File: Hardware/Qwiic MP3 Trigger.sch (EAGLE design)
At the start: 55 parts, among them J1 MICRO-SD, J3 PTH, J7 ISP, J8 3.5mm Audio, J9 Poke-Home, U1 TPA2005D1, U2 WT2003S, U3 AP2112-3.3V, U4 ATTINY84-ARDUINO

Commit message: File name clean up.
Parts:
- removed U$1: SPARKX-LOGO3, SparkX:SPARKX-LOGO3
- removed U$2: SPARKX-LOGO4, SparkX:SPARKX-LOGO4
- added LOGO2: SFE_LOGO_NAME.1_INCH, SparkFun-Aesthetics:SFE_LOGO_NAME.1_INCH
- added LOGO3: SFE_LOGO_NAME_FLAME.1_INCH, SparkFun-Aesthetics:SFE_LOGO_NAME_FLAME.1_INCH
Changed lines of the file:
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@@
 <class number="0" name="default" width="0" drill="0">
 </class>
-<class number="1" name="3.3V" width="0.1524" drill="0">
+<class number="1" name="3.3V" width="0.3048" drill="0">
 </class>
 </classes>
@@
 <part name="GND7" library="SparkFun-PowerSymbols" deviceset="GND" device=""/>
 <part name="FRAME1" library="SparkFun-Aesthetics" deviceset="FRAME-LETTER" device=""/>
-<part name="U$2" library="SparkX" deviceset="SPARKX-LOGO" device="4"/>
 <part name="SUPPLY8" library="SparkFun-PowerSymbols" deviceset="3.3V" device=""/>
 <part name="J4" library="SparkFun-Connectors" deviceset="QWIIC_CONNECTOR" device="JS-1MM"/>
 <part name="GND8" library="SparkFun-PowerSymbols" deviceset="GND" device=""/>
 <part name="LOGO1" library="SparkFun-Aesthetics" deviceset="OSHW-LOGO" device="MINI"/>
-<part name="U$1" library="SparkX" deviceset="SPARKX-LOGO" device="3" value="SPARKX-LOGO3"/>
 <part name="J5" library="SparkFun-Connectors" deviceset="CONN_01" device="PTH_NO_SILK_YES_STOP"/>
 <part name="JP1" library="SparkFun" deviceset="FIDUCIAL" device="UFIDUCIAL"/>
@@
 <part name="GND19" library="SparkFun-PowerSymbols" deviceset="GND" device=""/>
 <part name="GND20" library="SparkFun-PowerSymbols" deviceset="GND" device=""/>
+<part name="LOGO2" library="SparkFun-Aesthetics" deviceset="SFE_LOGO_NAME" device=".1_INCH"/>
+<part name="LOGO3" library="SparkFun-Aesthetics" deviceset="SFE_LOGO_NAME_FLAME" device=".1_INCH"/>
 </parts>
 <sheets>
@@
 <attribute name="DRAWING_NAME" x="162.814" y="17.78" size="2.7432" layer="94" font="vector"/>
 </instance>
-<instance part="U$2" gate="G$1" x="121.92" y="7.62" smashed="yes"/>
 <instance part="SUPPLY8" gate="G$1" x="48.26" y="27.94" smashed="yes" rot="MR0">
 <attribute name="VALUE" x="48.26" y="30.734" size="1.778" layer="96" rot="MR0" align="bottom-center"/>
@@
 </instance>
 <instance part="LOGO1" gate="G$1" x="121.92" y="22.86" smashed="yes"/>
-<instance part="U$1" gate="G$1" x="121.92" y="7.62" smashed="yes"/>
 <instance part="J5" gate="G$1" x="88.9" y="27.94" smashed="yes" rot="MR180">
 <attribute name="VALUE" x="86.36" y="32.766" size="1.778" layer="96" font="vector" rot="MR180"/>
@@
 <attribute name="VALUE" x="88.9" y="106.68" size="1.778" layer="96"/>
 </instance>
+<instance part="LOGO2" gate="G$1" x="2.286" y="42.926" smashed="yes"/>
+<instance part="LOGO3" gate="G$1" x="3.556" y="42.418" smashed="yes"/>
 </instances>
 <busses>
 </busses>
 <nets>
-<net name="3.3V" class="0">
+<net name="3.3V" class="1">
 <segment>
 <pinref part="J2" gate="G$1" pin="2"/>

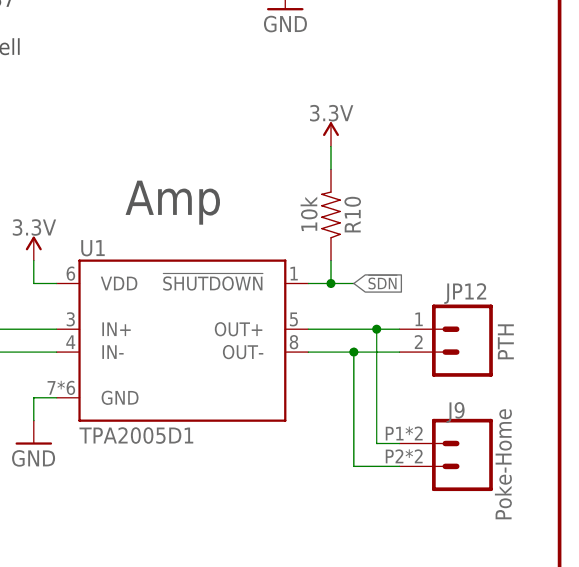
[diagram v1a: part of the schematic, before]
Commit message: Routing Playing pin on WS to Shutdown pin on amp
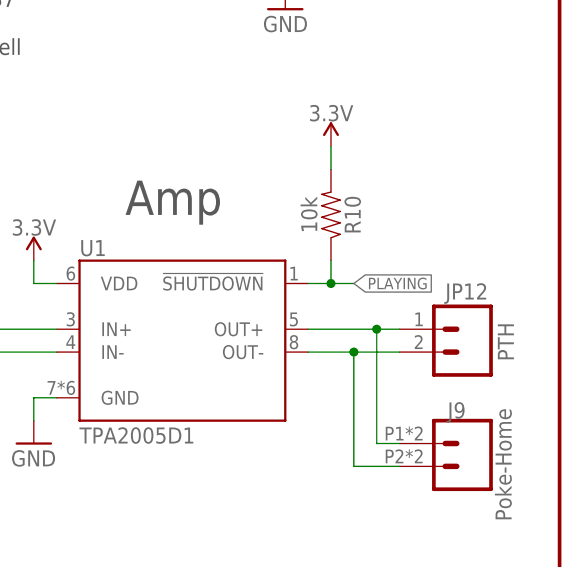
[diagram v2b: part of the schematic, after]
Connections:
- net !SDN: no longer R10.1, U1.!SHUTDOWN
- net PLAYING: now also R10.1, U1.!SHUTDOWN
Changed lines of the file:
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@@
 <net name="!SDN" class="0">
-<segment>
-<wire x1="226.06" y1="73.66" x2="223.52" y2="73.66" width="0.1524" layer="91"/>
-<wire x1="223.52" y1="73.66" x2="220.98" y2="73.66" width="0.1524" layer="91"/>
-<wire x1="223.52" y1="76.2" x2="223.52" y2="73.66" width="0.1524" layer="91"/>
-<junction x="223.52" y="73.66"/>
-<pinref part="R10" gate="G$1" pin="1"/>
-<label x="226.06" y="73.66" size="1.27" layer="95" rot="MR180" xref="yes"/>
-<pinref part="U1" gate="U1" pin="!SHUTDOWN"/>
-</segment>
 <segment>
 <pinref part="U2" gate="U1" pin="P10"/>
@@
 <pinref part="U4" gate="U1" pin="(A2)2"/>
 </segment>
+<segment>
+<wire x1="226.06" y1="73.66" x2="223.52" y2="73.66" width="0.1524" layer="91"/>
+<wire x1="223.52" y1="73.66" x2="220.98" y2="73.66" width="0.1524" layer="91"/>
+<wire x1="223.52" y1="76.2" x2="223.52" y2="73.66" width="0.1524" layer="91"/>
+<junction x="223.52" y="73.66"/>
+<pinref part="R10" gate="G$1" pin="1"/>
+<label x="226.06" y="73.66" size="1.27" layer="95" rot="MR180" xref="yes"/>
+<pinref part="U1" gate="U1" pin="!SHUTDOWN"/>
+</segment>
 </net>

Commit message: Rolling to v11 copper
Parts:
- added JP8: INT, SparkFun-Jumpers:JUMPER-SMT_2_NC_TRACE_SILK
- added R7: 10k, SparkFun-Resistors:10KOHM-0603-1/10W-1%
- JP7: device SparkFun-Jumpers:JUMPER-SMT_2_NO_NO-SILK -> SparkFun-Jumpers:JUMPER-SMT_2_NO_SILK
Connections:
- new net N$4: JP8.1, R7.2
- net !INT: now also R7.1
- net 3.3V: now also JP8.2
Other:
- moved on the sheet: C16, C2, J7, JP7, JP9, R2, R6, R8, U3, U4

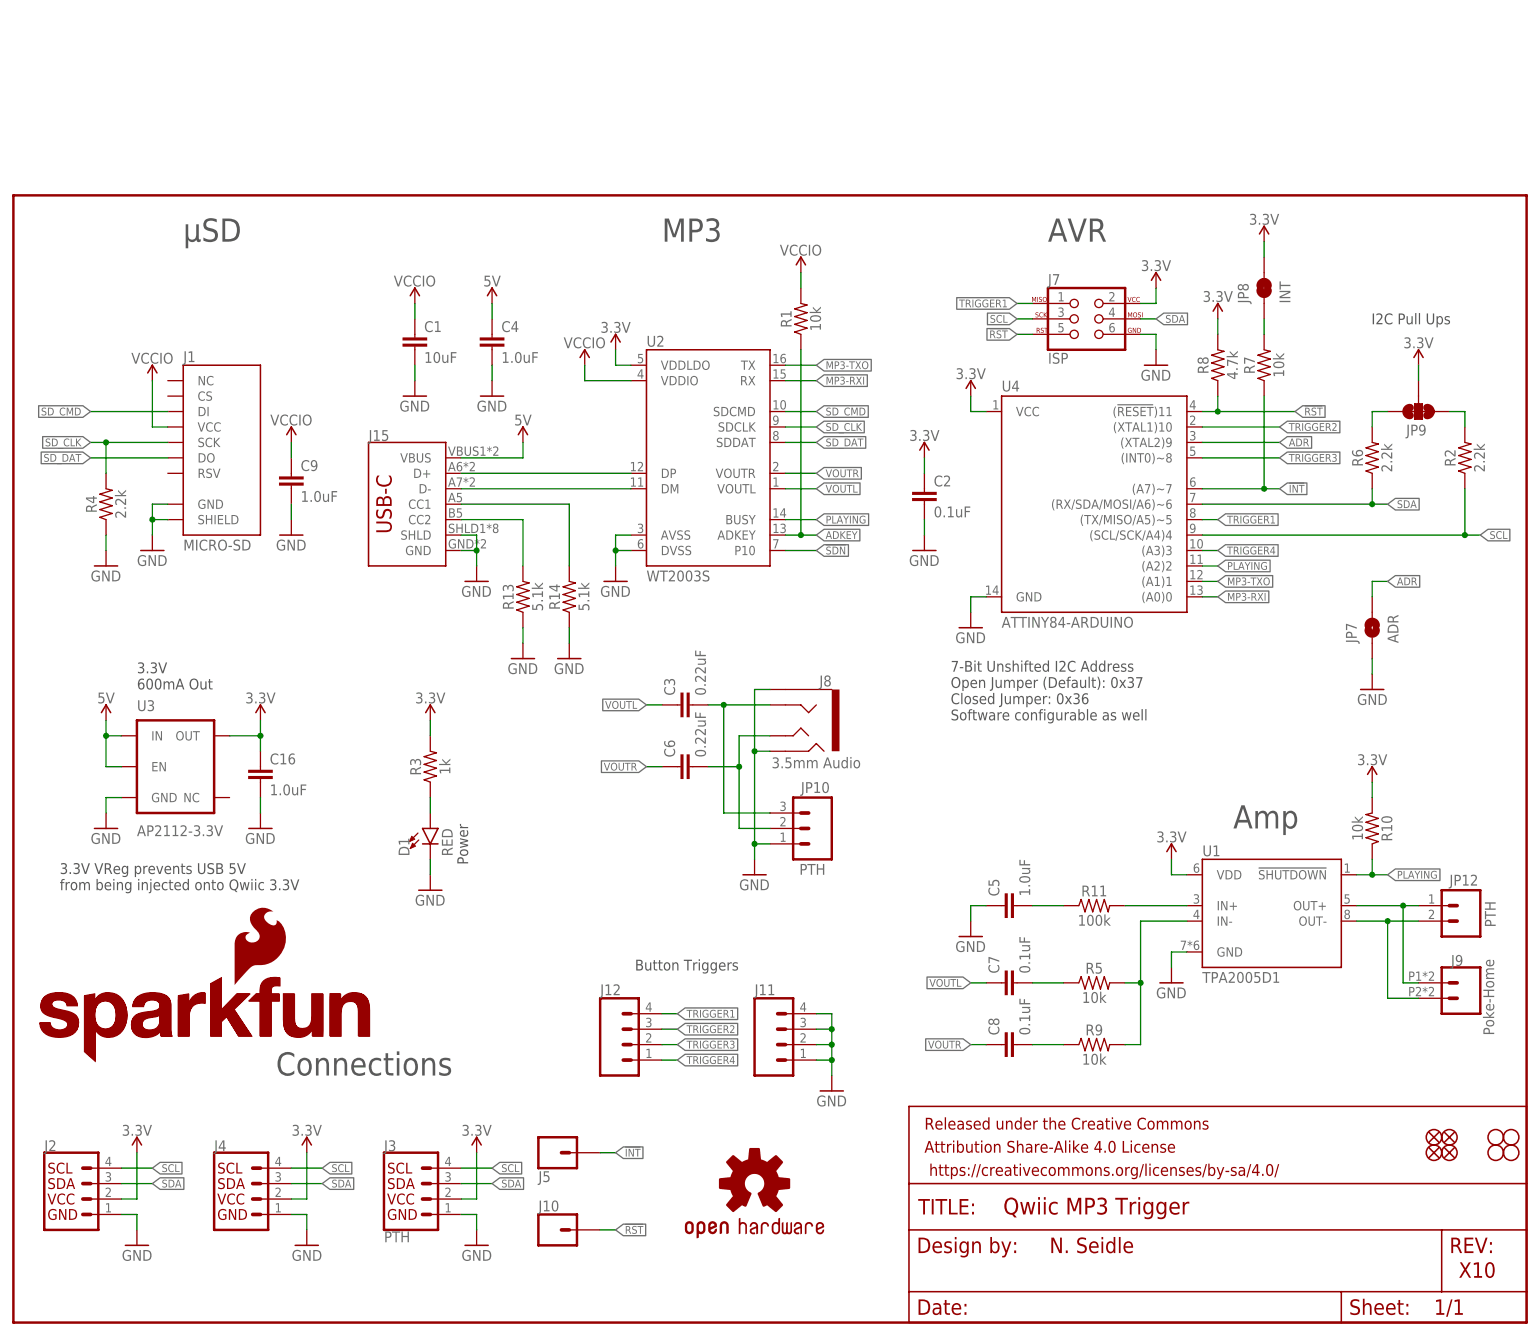
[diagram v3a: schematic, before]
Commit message: Re-route to accommodate H4
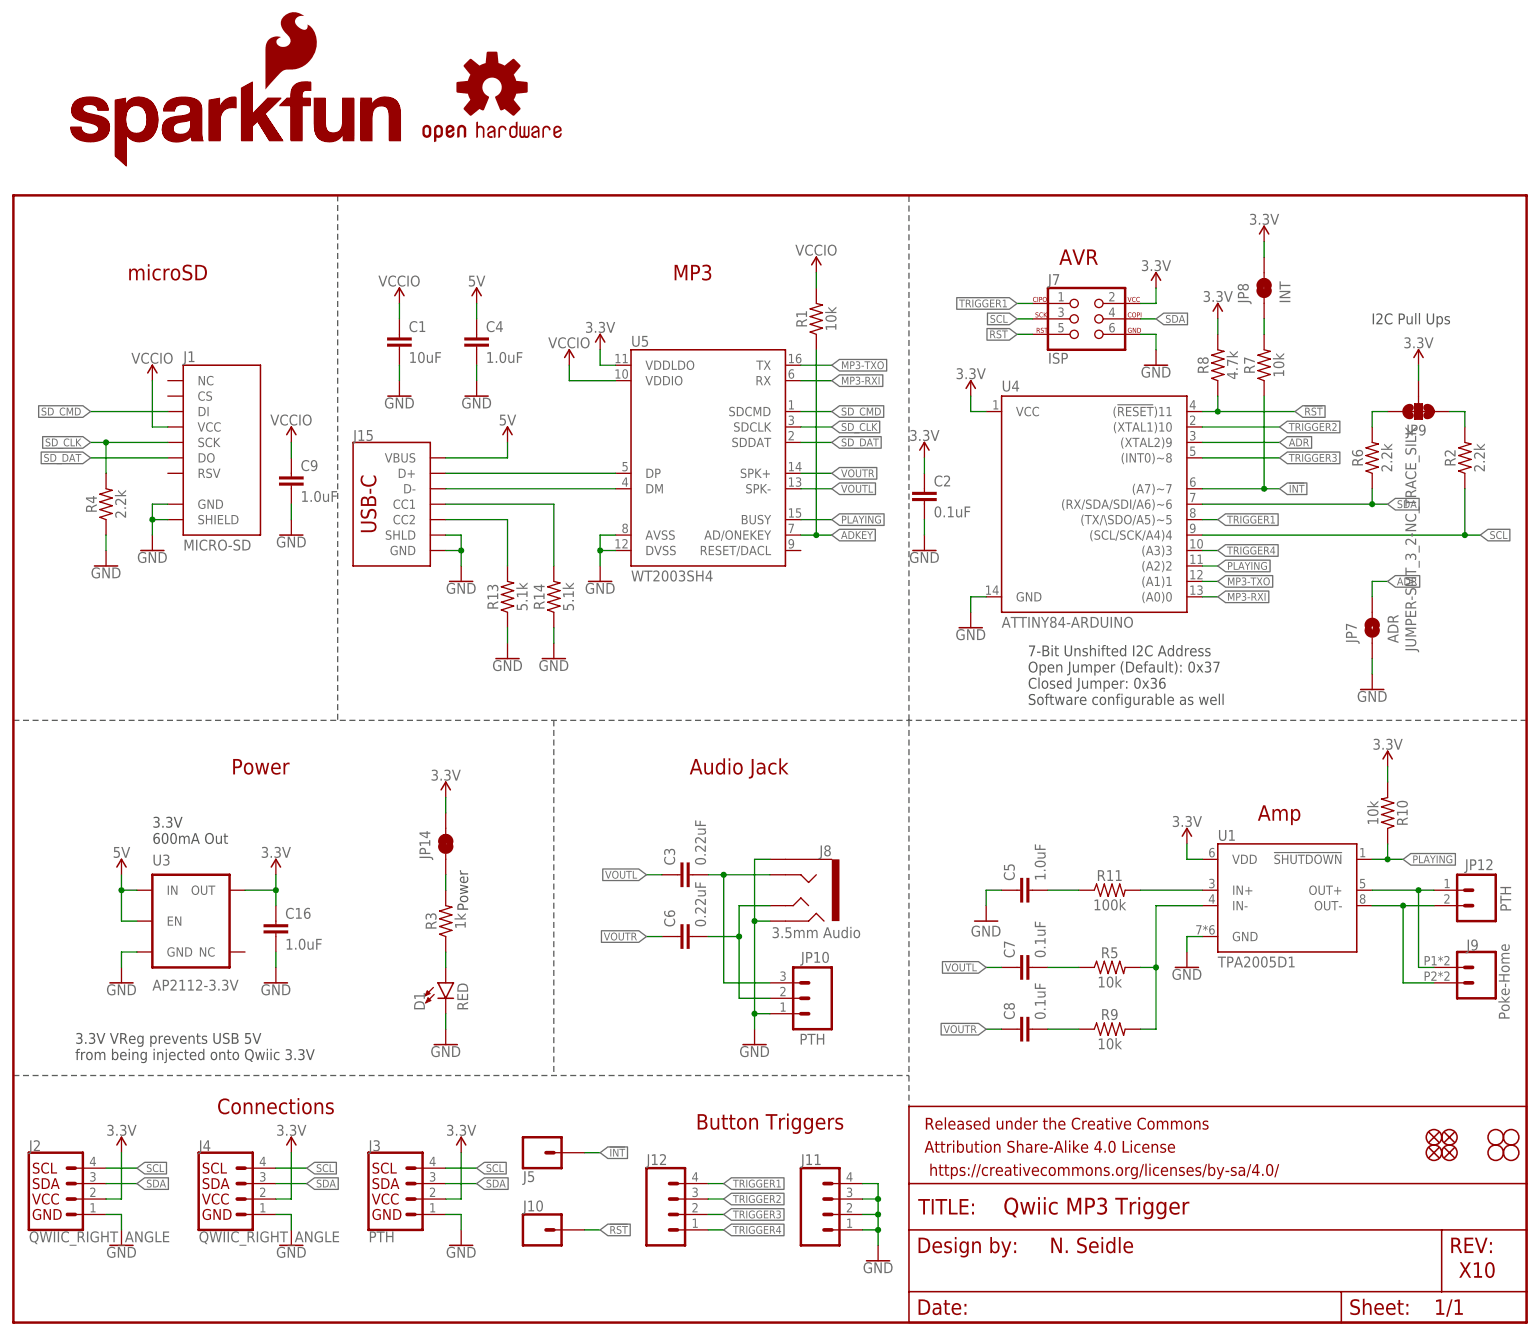
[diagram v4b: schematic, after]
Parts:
- removed U2: WT2003S, WT2003S:WT2003S
- added JP14: JUMPER-SMT_2_NC_TRACE_SILK, SparkFun-Jumpers:JUMPER-SMT_2_NC_TRACE_SILK
- added U5: WT2003SH4, SparkFun-IC-Special-Function:WT2003SH4
- J15: device SparkFun-Connectors:USB_C16PIN -> SparkFun-Connectors:USB_C_2-LAYER_PADS
- J2, J4: value (none) -> QWIIC_RIGHT_ANGLE
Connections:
- removed net !SDN: U2.P10
- new net N$6: JP14.1, R3.2
- net 3.3V: now also JP14.2, U5.VDDLDO; no longer R3.2, U2.VDDLDO
- net ADKEY: now also U5.AD/ONEKEY; no longer U2.ADKEY
- net D+: now also U5.DP; no longer U2.DP
- net D-: now also U5.DM; no longer U2.DM
- net GND: now also U5.AVSS, U5.DVSS; no longer U2.AVSS, U2.DVSS
- net MP3-RXI: now also U5.RX; no longer U2.RX
- net MP3-TXO: now also U5.TX; no longer U2.TX
- net PLAYING: now also U5.BUSY; no longer U2.BUSY
- net SDA: now also U4.(RX/SDA/SDI/A6)~6; no longer U4.(RX/SDA/MOSI/A6)~6
- net SD_CLK: now also U5.SDCLK; no longer U2.SDCLK
- net SD_CMD: now also U5.SDCMD; no longer U2.SDCMD
- net SD_DAT: now also U5.SDDAT; no longer U2.SDDAT
- net TRIGGER1: now also U4.(TX/\SDO/A5)~5; no longer U4.(TX/MISO/A5)~5
- net VCCIO: now also U5.VDDIO; no longer U2.VDDIO
- net VOUTL: now also U5.SPK-; no longer U2.VOUTL
- net VOUTR: now also U5.SPK+; no longer U2.VOUTR
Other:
- note added: "Audio Jack"
- note added: "microSD"
- note removed: "μSD"
- moved on the sheet: C1, C16, C3, C4, C5, C6, C7, C8, D1, J10, J2, J3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

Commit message: Add pop reduction component changes from v12.
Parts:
- C5: value 1.0uF -> 22nF; device SparkFun-Capacitors:1.0UF-0603-16V-10% -> SparkFun-Capacitors:22NF/22,000PF-0603-25V-10%-X7R
- C7, C8: value 0.1uF -> 10nF; device SparkFun-Capacitors:0.1UF-0603-25V-(+80/-20%) -> SparkFun-Capacitors:10NF-0603-50V-10%
- R11: value 100k -> 47k; device SparkFun-Resistors:100KOHM-0603-1/10W-1% -> SparkFun-Resistors:47KOHM-0603-1/10W-1%
- R5, R9: value 10k -> 100k; device SparkFun-Resistors:10KOHM-0603-1/10W-1% -> SparkFun-Resistors:100KOHM-0603-1/10W-1%
- R8: value 4.7k -> 10k; device SparkFun-Resistors:4.7KOHM-0603-1/10W-1% -> SparkFun-Resistors:10KOHM-0603-1/10W-1%
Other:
- note added: "v20"
- note removed: "X10"
- moved on the sheet: C5, C7, C8, C9, J1

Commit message: Proto with MY1690
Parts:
- removed J1: MICRO-SD, SparkFun-Connectors:MICRO-SD_CARD_SOCKETPUSH-PUSH
- removed U5: WT2003SH4, SparkFun-IC-Special-Function:WT2003SH4
- added J14: MICRO-SD, SparkFun-Connectors:MICRO-SD-PUSH-PUSH-EXT-PIN
- added LOGO4: QWIIC_LOGO_CONNECTOR, SparkFun-Aesthetics:QWIIC_LOGO_CONNECTOR
- added U2: MY1690-16S, MY1690:MY1690-16S
- C1: value 10uF -> 1.0uF; device SparkFun-Capacitors:10UF-0603-6.3V-20% -> SparkFun-Capacitors:1.0UF-0603-16V-10%-X7R
- C5: device SparkFun-Capacitors:22NF/22,000PF-0603-25V-10%-X7R -> SparkFun-Capacitors:22NF/22,000PF-0603-50V-10%
- FRAME1: value FRAME-LETTER -> FRAME-LEDGER; device SparkFun-Aesthetics:FRAME-LETTER -> SparkFun-Aesthetics:FRAME-LEDGER
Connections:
- new net N$7: C4.1, U2.VPN
- net 3.3V: now also U2.VCC; no longer U5.VDDLDO
- net 5V: now also C1.1; no longer C4.1
- net ADKEY: now also U2.ADKEY; no longer U5.AD/ONEKEY
- net D+: now also U2.DP; no longer U5.DP
- net D-: now also U2.DM; no longer U5.DM
- net GND: now also J14.GND, U2.GND; no longer J1.GND, J1.SHIELD, U5.AVSS, U5.DVSS
- net MP3-RXI: now also U2.RX; no longer U5.RX
- net MP3-TXO: now also U2.TX; no longer U5.TX
- net PLAYING: now also U2.BUSY; no longer U5.BUSY
- net SD_CLK: now also J14.CLK/SCK, U2.SDCLK; no longer J1.SCK, U5.SDCLK
- net SD_CMD: now also J14.CMD/SDI, U2.SDCMD; no longer J1.DI, U5.SDCMD
- net SD_DAT: now also J14.DAT0/SDO, U2.SDDAT; no longer J1.DO, U5.SDDAT
- net VCCIO: now also J14.VCC, U2.3V3-O; no longer C1.1, J1.VCC, U5.VDDIO
- net VOUTL: now also U2.DACL; no longer U5.SPK-
- net VOUTR: now also U2.DACR; no longer U5.SPK+
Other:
- note added: "Fix headphone labels, L is actually R"
- note added: "v30"
- note removed: "v20"
- moved on the sheet: C1, C2, C4, C5, C7, C8, C9, J15, J7, J9, JP12, JP7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

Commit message: Route MY1690X-16S
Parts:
- removed R1: 10k, SparkFun-Resistors:10KOHM-0603-1/10W-1%
- removed U2: MY1690-16S, MY1690:MY1690-16S
- added C10: 2.2uF, SparkFun-Capacitors:2.2UF-0603-10V-20%
- added J1: (no value), SparkFun-Connectors:CONN_01PTH_NO_SILK_YES_STOP
- added U5: MY1690X-16S, MY1690X-16S:MY1690X-16S
- C4: value 1.0uF -> 2.2uF; device SparkFun-Capacitors:1.0UF-0603-16V-10% -> SparkFun-Capacitors:2.2UF-0603-10V-20%
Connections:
- removed net ADKEY: R1.1, U2.ADKEY
- new net N$10: C10.1, U5.VCOM
- net 3.3V: now also U5.VCC; no longer U2.VCC
- net 5V: now also J1.1
- net D+: now also U5.DP; no longer U2.DP
- net D-: now also U5.DM; no longer U2.DM
- net GND: now also C10.2, U5.GND; no longer U2.GND
- net MP3-RXI: now also U5.RX; no longer U2.RX
- net MP3-TXO: now also U5.TX; no longer U2.TX
- net N$7: now also U5.VPN; no longer U2.VPN
- net PLAYING: now also U5.BUSY; no longer U2.BUSY
- net SD_CLK: now also U5.SDCLK; no longer U2.SDCLK
- net SD_CMD: now also U5.SDCMD; no longer U2.SDCMD
- net SD_DAT: now also U5.SDDAT; no longer U2.SDDAT
- net VCCIO: now also U5.3V3-O; no longer R1.2, U2.3V3-O
- net VOUTL: now also U5.DACL; no longer U2.DACL
- net VOUTR: now also U5.DACR; no longer U2.DACR
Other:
- note added: "v20"
- note removed: "Fix headphone labels, L is actually R"
- note removed: "v30"
- moved on the sheet: C1, C16, C2, C3, C4, C5, C6, C7, C8, C9, D1, J10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
